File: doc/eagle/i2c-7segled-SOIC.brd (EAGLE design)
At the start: 65 x 56 mm, 16 parts

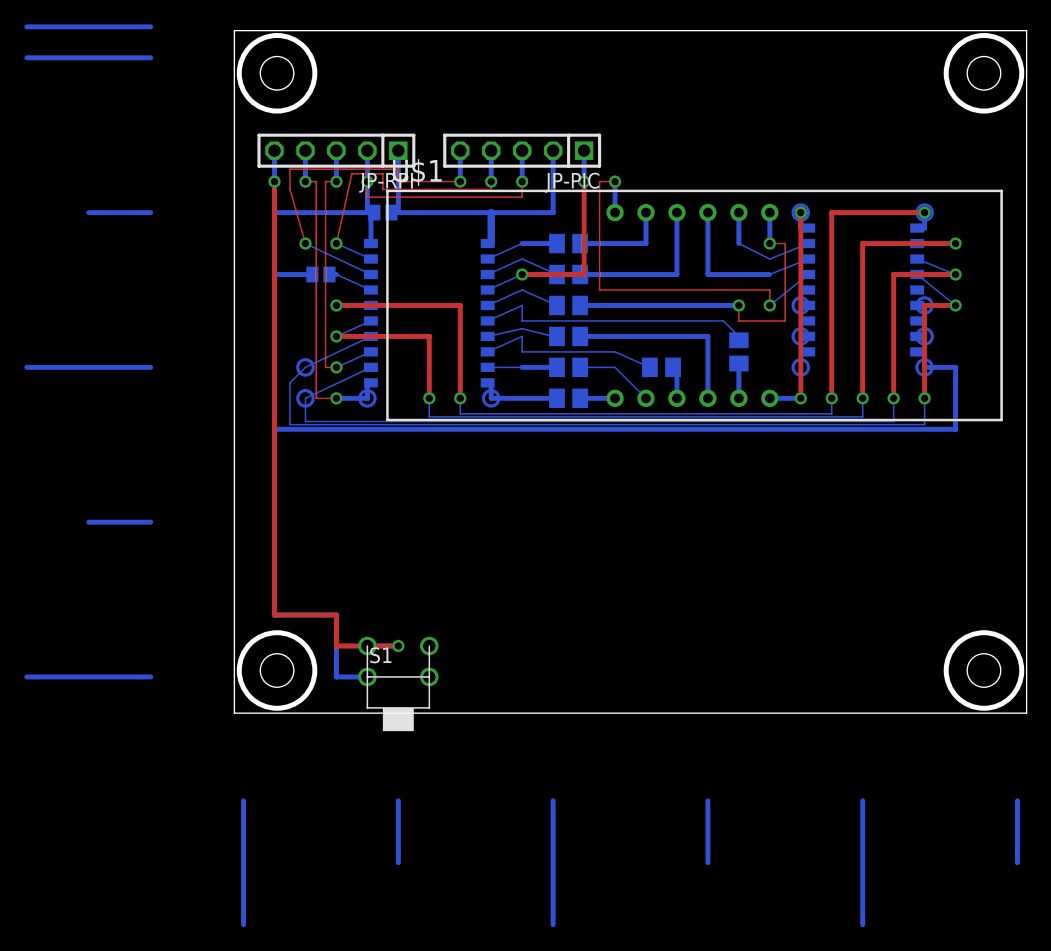
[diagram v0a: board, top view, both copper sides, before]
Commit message: remove unnecessary wires for borad documents
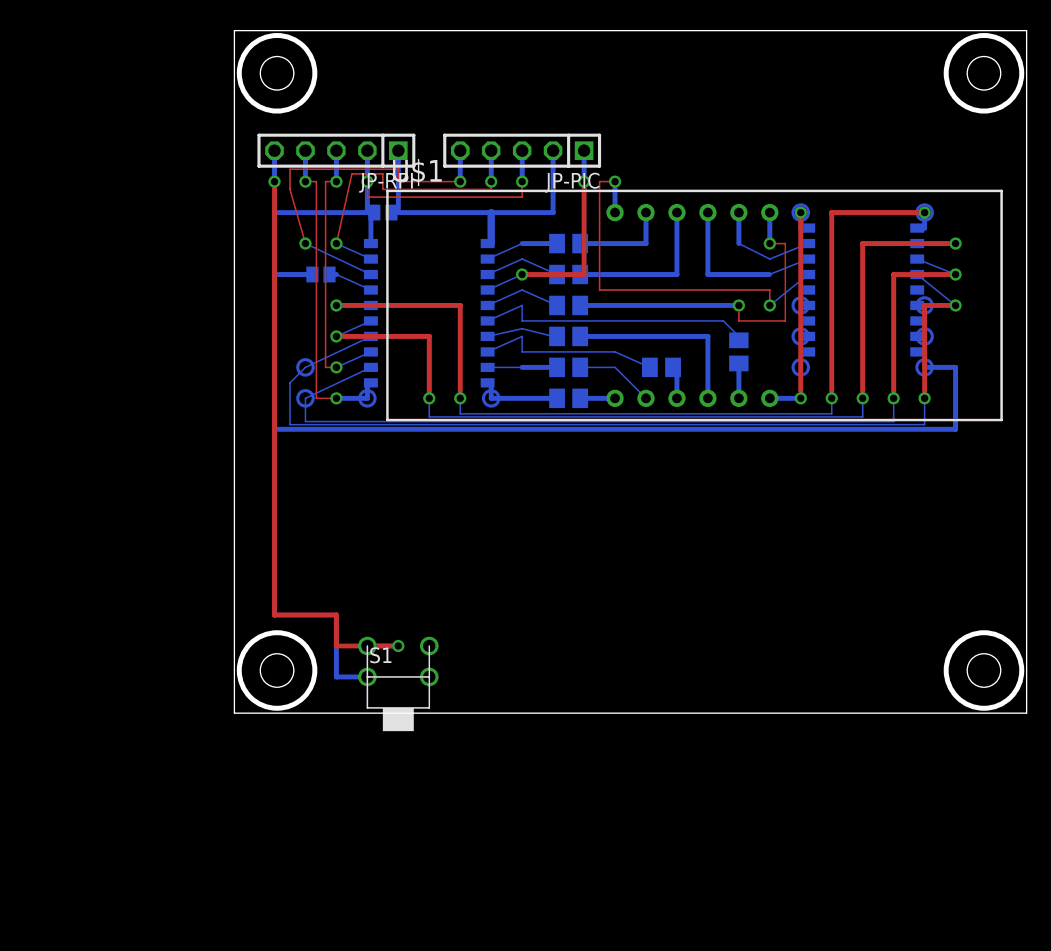
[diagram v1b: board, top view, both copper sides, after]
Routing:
- net N$44: track 10.2 -> 0.00 mm
- net N$43: track 10.2 -> 0.00 mm
- net N$41: track 10.2 -> 0.00 mm
- net N$39: track 10.2 -> 0.00 mm
- net N$37: track 10.2 -> 0.00 mm
- net N$35: track 10.2 -> 0.00 mm
- net N$33: track 10.2 -> 0.00 mm
- net N$42: track 5.08 -> 0.00 mm
- net N$40: track 5.08 -> 0.00 mm
- net N$38: track 5.08 -> 0.00 mm
- net N$36: track 5.08 -> 0.00 mm
- net N$34: track 5.08 -> 0.00 mm
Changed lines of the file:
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@@
 <via x="17.78" y="43.18" extent="1-16" drill="0.6" shape="square"/>
-</signal>
-<signal name="N$33">
-<wire x1="0" y1="-7.62" x2="0" y2="-17.78" width="0.4064" layer="16"/>
-</signal>
-<signal name="N$34">
-<wire x1="12.7" y1="-7.62" x2="12.7" y2="-12.7" width="0.4064" layer="16"/>
-</signal>
-<signal name="N$35">
-<wire x1="25.4" y1="-7.62" x2="25.4" y2="-17.78" width="0.4064" layer="16"/>
-</signal>
-<signal name="N$36">
-<wire x1="38.1" y1="-7.62" x2="38.1" y2="-12.7" width="0.4064" layer="16"/>
-</signal>
-<signal name="N$37">
-<wire x1="50.8" y1="-7.62" x2="50.8" y2="-17.78" width="0.4064" layer="16"/>
-</signal>
-<signal name="N$38">
-<wire x1="63.5" y1="-7.62" x2="63.5" y2="-12.7" width="0.4064" layer="16"/>
-</signal>
-<signal name="N$39">
-<wire x1="-7.62" y1="2.54" x2="-17.78" y2="2.54" width="0.4064" layer="16"/>
-</signal>
-<signal name="N$40">
-<wire x1="-7.62" y1="15.24" x2="-12.7" y2="15.24" width="0.4064" layer="16"/>
-</signal>
-<signal name="N$41">
-<wire x1="-7.62" y1="27.94" x2="-17.78" y2="27.94" width="0.4064" layer="16"/>
-</signal>
-<signal name="N$42">
-<wire x1="-7.62" y1="40.64" x2="-12.7" y2="40.64" width="0.4064" layer="16"/>
-</signal>
-<signal name="N$43">
-<wire x1="-7.62" y1="53.34" x2="-17.78" y2="53.34" width="0.4064" layer="16"/>
-</signal>
-<signal name="N$44">
-<wire x1="-7.62" y1="55.88" x2="-17.78" y2="55.88" width="0.4064" layer="16"/>
 </signal>
 <signal name="N$6">

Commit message: update eagle documents
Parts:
- added U$3: (no value), frames:A4L-LOC
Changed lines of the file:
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@@
 <element name="U$2" library="toshiba-td62083" package="SO18" value="TD62083" x="51.435" y="34.29" rot="MR270"/>
 <element name="S1" library="switch-custom" package="2X1SIDE" value="2X1SIDE" x="12.7" y="2.54"/>
+<element name="U$3" library="frames" package="A4L-LOC" value="" x="-91.44" y="-63.5"/>
 </elements>
 <signals>
